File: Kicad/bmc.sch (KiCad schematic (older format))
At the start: 30 parts, among them J1101 Header, J1102 Header, J1103 Conn_01x05, J1104 Double-mini-DIN-6, SW1101 SW_DIP_x01, SW1102 SW_DIP_x01, U1101 STM32F031K6T6

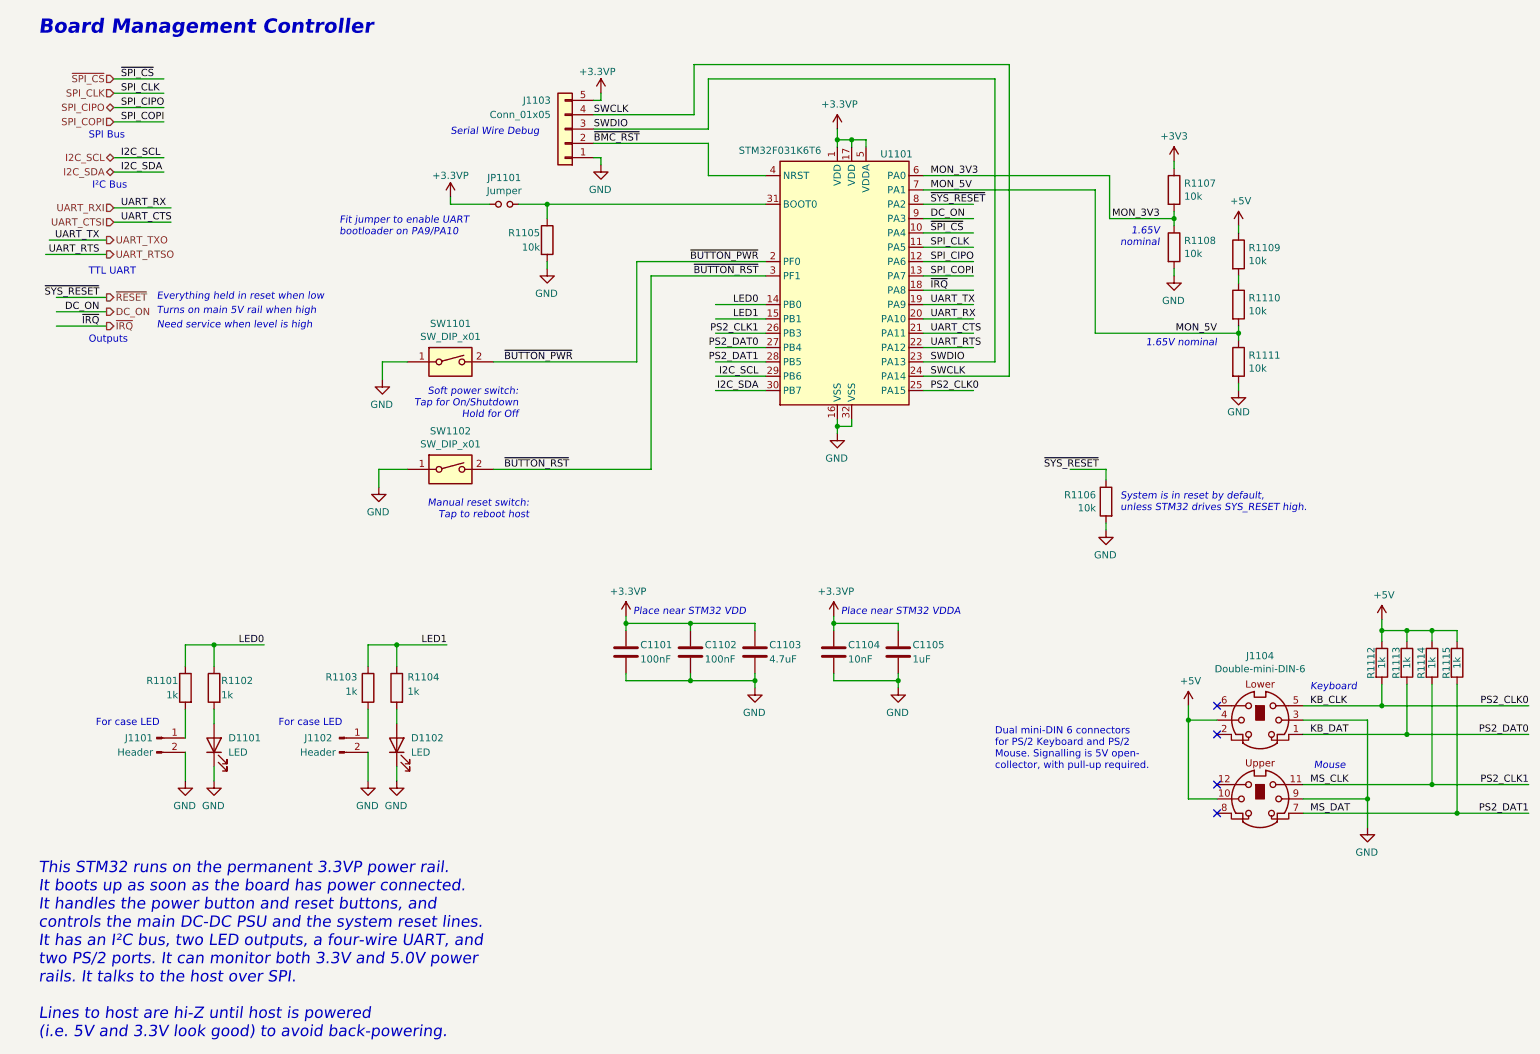
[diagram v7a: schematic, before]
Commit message: Added expansion header.
Involved rerouting quite a few things.
Also added through-hole switches for power/reset.
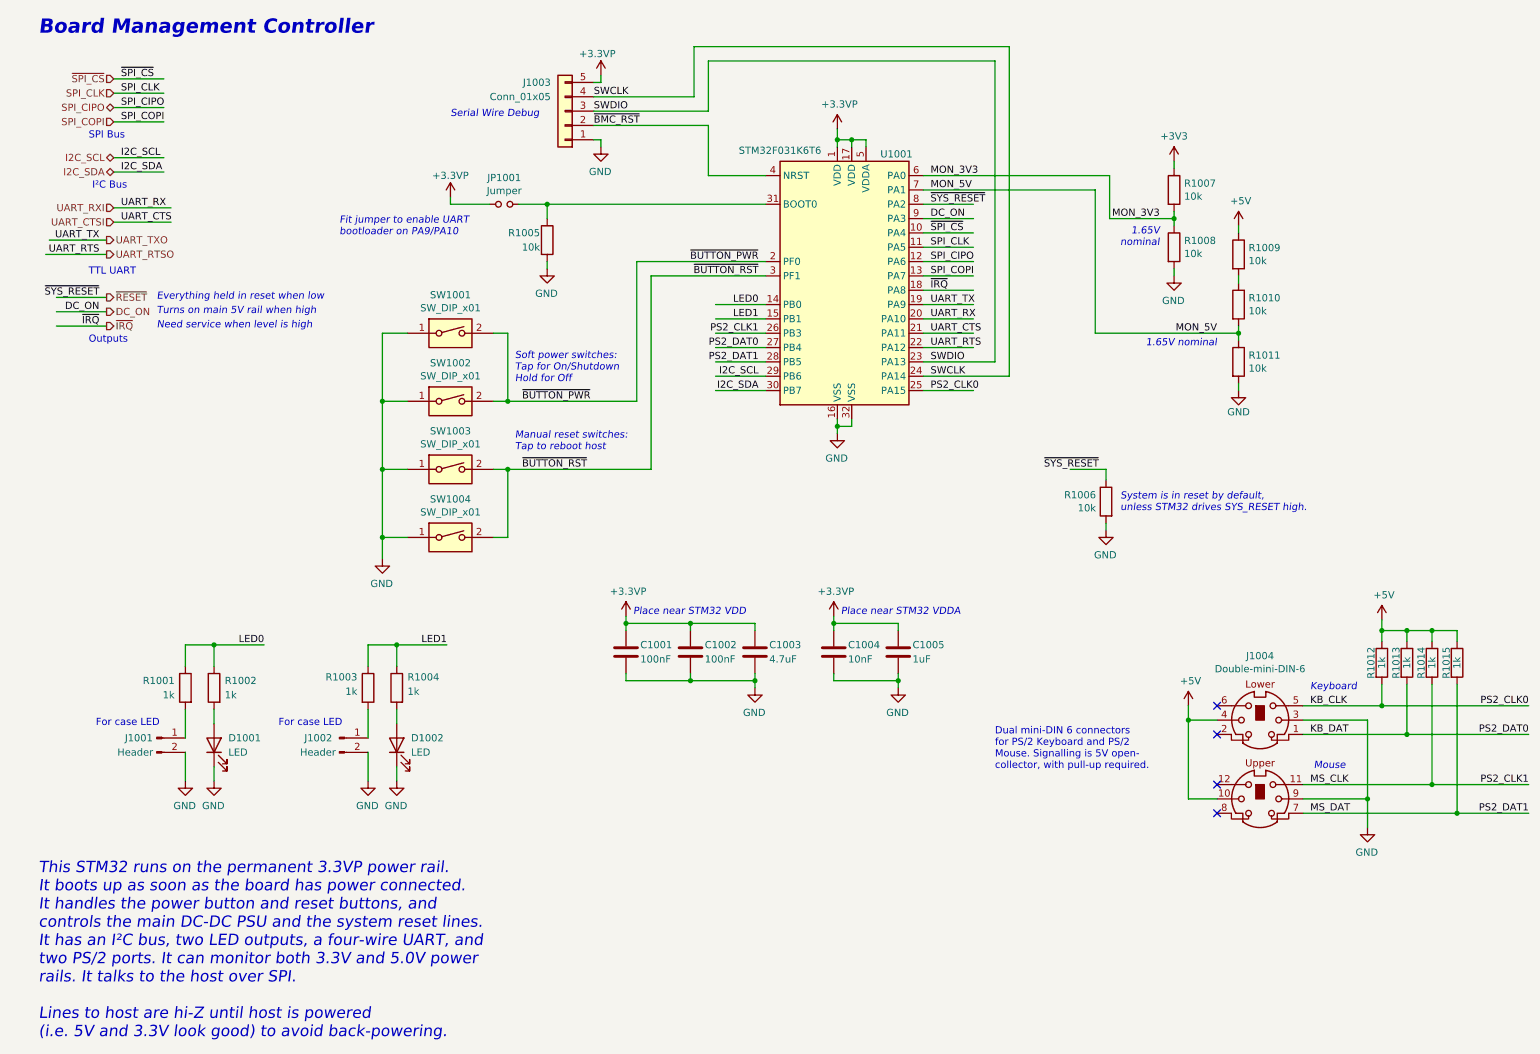
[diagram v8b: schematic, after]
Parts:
- added SW1001, SW1004: SW_DIP_x01, Button_Switch_THT:SW_PUSH_6mm, symbol Switch:SW_DIP_x01
- renumbered C1101 to C1001, C1102 to C1002, C1103 to C1003, C1104 to C1004, C1105 to C1005, D1101 to D1001, D1102 to D1002, J1101 to J1001, J1102 to J1002, J1103 to J1003, J1104 to J1004, JP1101 to JP1001, R1101 to R1001, R1102 to R1002, R1103 to R1003, R1104 to R1004, R1105 to R1005, R1106 to R1006, R1107 to R1007, R1108 to R1008, R1109 to R1009, R1110 to R1010, R1111 to R1011, R1112 to R1012, R1113 to R1013, R1114 to R1014, R1115 to R1015, SW1101 to SW1002, SW1102 to SW1003, U1101 to U1001
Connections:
- wire segments 157 -> 167
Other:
- note added: "Manual reset switches:\nTap to reboot host"
- note added: "Soft power switches:\nTap for On/Shutdown\nHold for Off"
- note removed: "Manual reset switch:\nTap to reboot host"
- note removed: "Soft power switch:\nTap for On/Shutdown\nHold for Off"
- moved on the sheet: J1003, SW1002
